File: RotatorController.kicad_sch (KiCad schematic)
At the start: 58 parts, among them J1 USB_A, J2 Rotator, J4 Motor Cap, K1 G5LE-1, K2 G5LE-1, K3 G5LE-1, Q1 BSS123, Q2 BSS123, Q3 BSS123, SW1 CW, SW2 CW, U1 Teensy4.0, U3 AP2161W

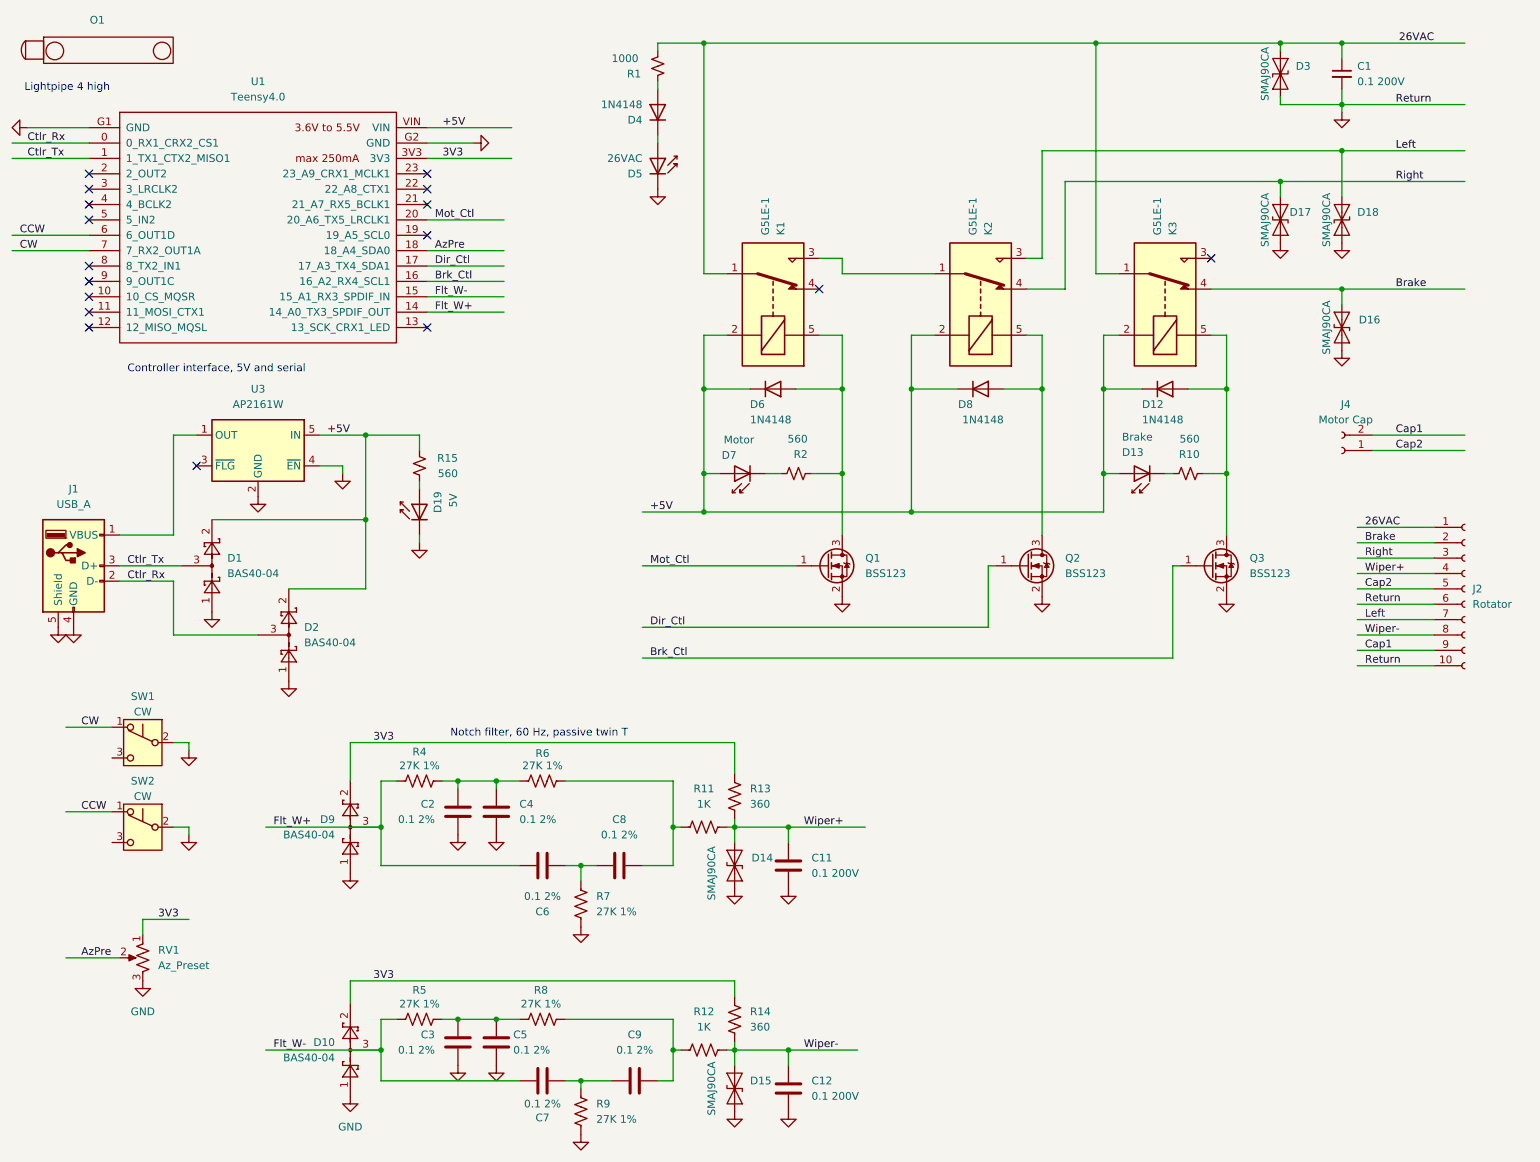
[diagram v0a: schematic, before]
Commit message: Created V3 branch for new board with 3.6V zeners for protection
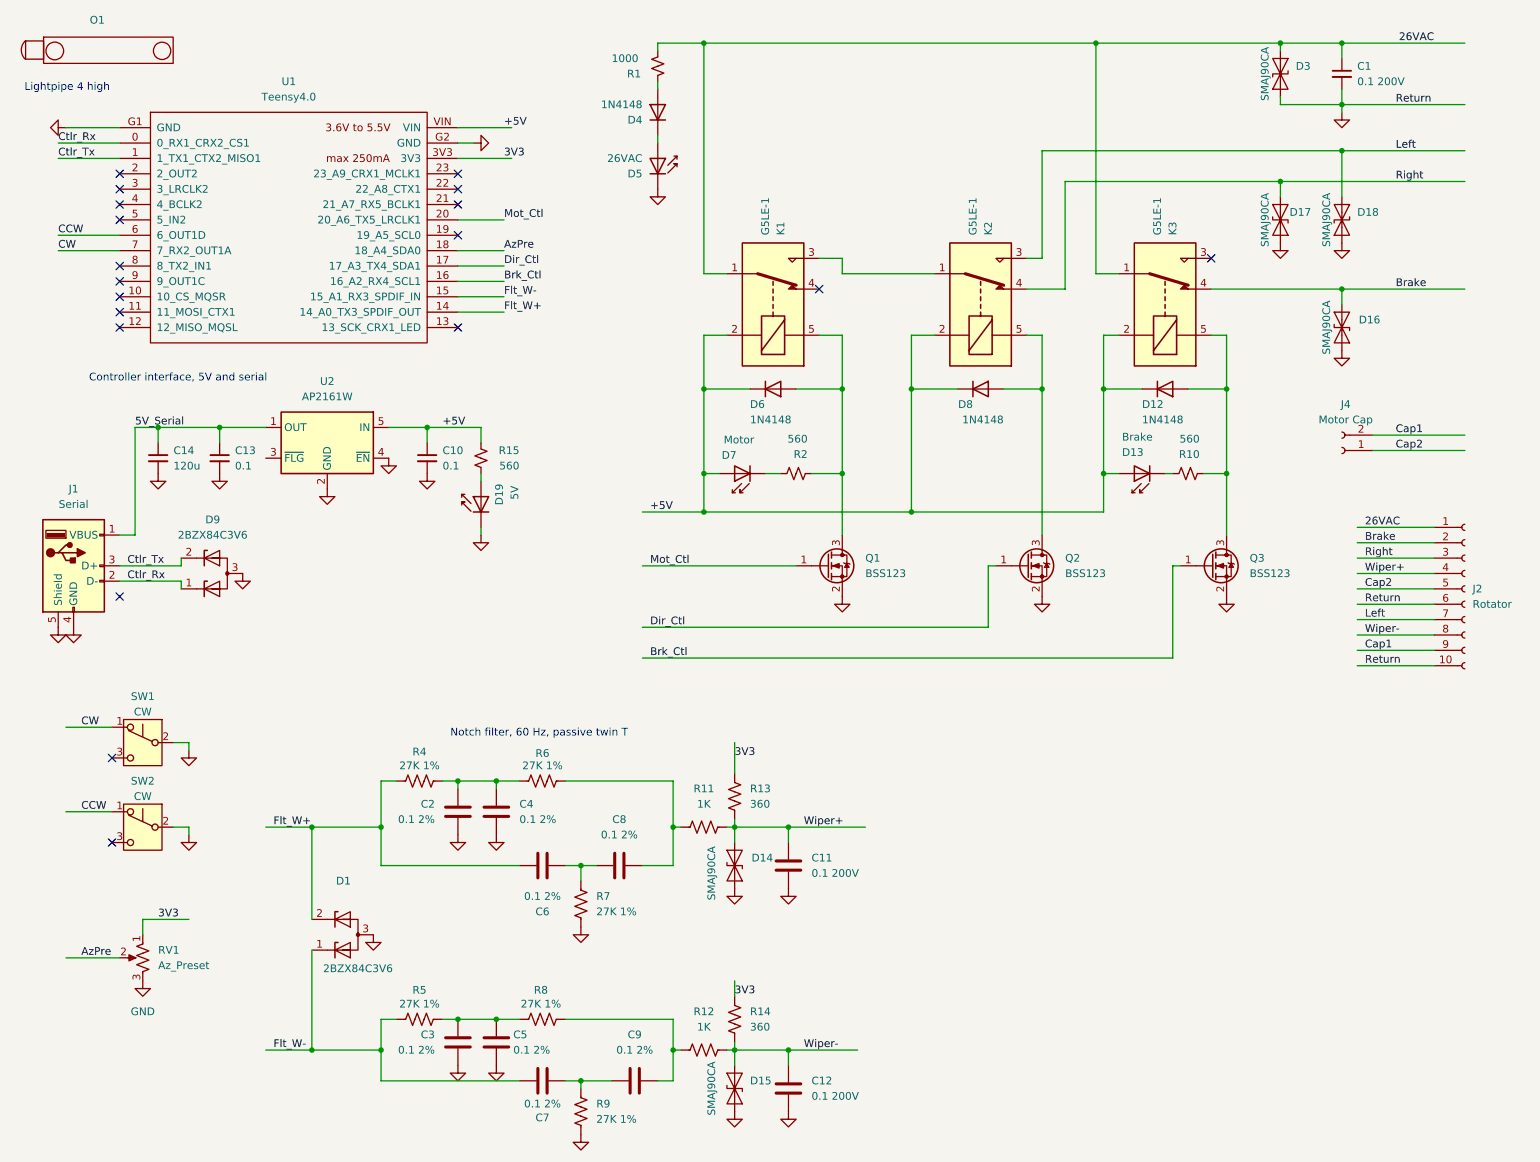
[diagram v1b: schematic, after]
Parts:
- removed D1, D10, D2, D9: BAS40-04, Package_TO_SOT_SMD:SOT-23, symbol Diode:BAS40-04
- removed U3: AP2161W, Package_TO_SOT_SMD:SOT-23-5, symbol Power_Management:AP2161W
- added C10, C13: 0.1, Capacitor_SMD:C_1206_3216Metric_Pad1.33x1.80mm_HandSolder, symbol Device:C_Small
- added C14: 120u, Capacitor_SMD:C_1206_3216Metric_Pad1.33x1.80mm_HandSolder, symbol Device:C_Small
- added D1, D9: 2BZX84C3V6, Package_TO_SOT_SMD:SOT-23, symbol Diode:MMBZxx
- added U2: AP2161W, Package_TO_SOT_SMD:SOT-23-5, symbol Power_Management:AP2161W
- D12, D4, D6, D8: footprint Diode_THT:D_DO-35_SOD27_P7.62mm_Horizontal -> Diode_SMD:D_SOD-123F
- D13, D19, D5, D7: footprint LED_THT:LED_D3.0mm_IRBlack -> LED_SMD:LED_0805_2012Metric
- J1: value USB_A -> Serial
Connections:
- net +5V: now also C10.1, U2.5 (IN)
- net Ctlr_Rx: now also D9.1 (K)
- net Ctlr_Tx: now also D9.2 (K)
- net Flt_W+: now also D1.2 (K)
- net Flt_W-: now also D1.1 (K)
- net GND: now also C10.2, C13.2, C14.2, D1.3 (A), D9.3 (A), U2.2 (GND), U2.4 (~{EN})
- net 5V_Serial: now reaches J1.1 (VBUS)
- net 5V_Serial: now also C13.1, C14.1, U2.1 (OUT)
- no-connect marks 17 -> 19
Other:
- moved on the sheet: D19, R15
